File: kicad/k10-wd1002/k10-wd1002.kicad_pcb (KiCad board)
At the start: 2 copper layers, 139.7 x 114.3 mm, 10 parts, among them J1 J1 - Kaypro, J2 J2 - WD1002-HDO, U1 74LS00, U2 74LS138

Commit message: Refine K10-WD1002 PCB layout
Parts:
- moved J2 2.54 mm to (181.6, 142.2)
- moved C1 2.54 mm to (113.0, 91.4)
- moved J1 2.54 mm to (87.6, 127.0)
- moved R1 2.54 mm to (124.5, 94.0)
- moved U1 2.54 mm to (133.3, 94.0)
- moved U2 2.54 mm to (100.3, 91.4)
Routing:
- net (no net): track 3407.3 -> 3405.9 mm
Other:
- board text added: "1"
- board text added: "40"
- board text added: "50"
- board text added: "81-212A (2022)"
- board text added: "C1"
- board text added: "J1"
- board text added: "J2"
- board text added: "KAYPRO"
- board text added: "R1"
- board text added: "U1"
- board text added: "U2"
- board text added: "WD1002-05/HDO"

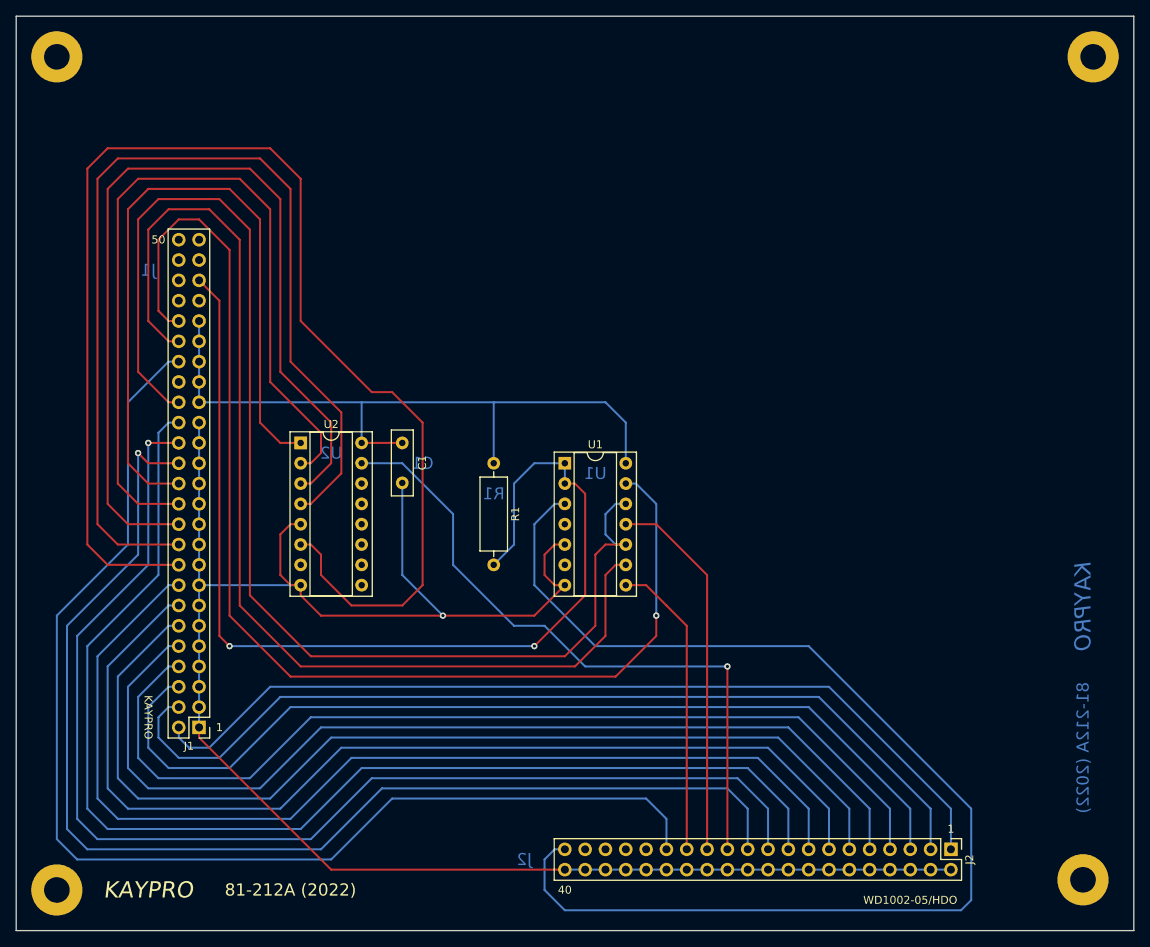
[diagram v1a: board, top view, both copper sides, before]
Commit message: Finish PCB layout
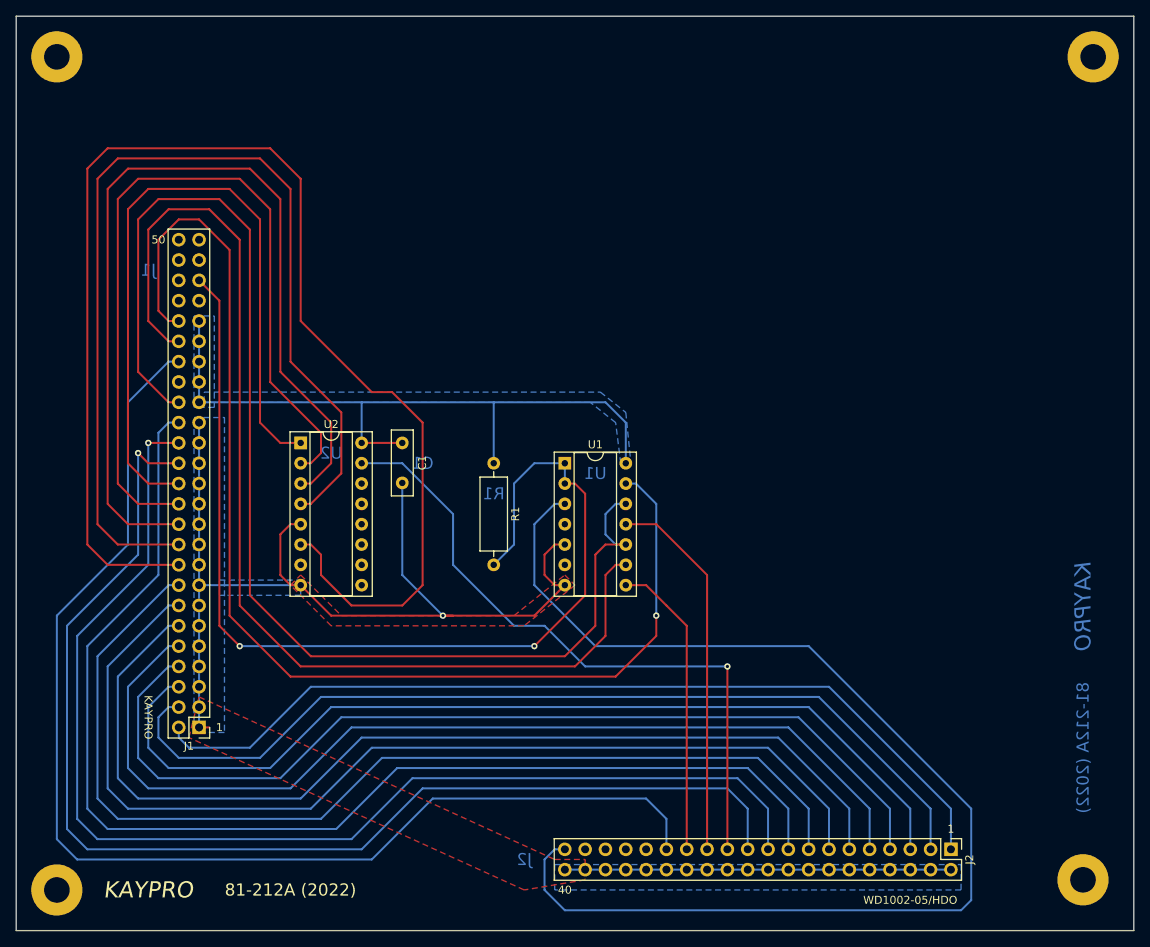
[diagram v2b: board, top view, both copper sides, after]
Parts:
- C1: value 0.1uF -> 0.1
- J1: value J1 - Kaypro -> Kaypro
- J2: value J2 - WD1002-HDO -> WD1002
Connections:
- C1 pad 1: (no net) -> VCC
- C1 pad 2: (no net) -> GND
- J1 pad 1: (no net) -> GND
- J1 pad 10: (no net) -> /BD4
- J1 pad 11: (no net) -> GND
- J1 pad 12: (no net) -> /BD5
- J1 pad 13: (no net) -> GND
- J1 pad 14: (no net) -> /BD6
- J1 pad 15: (no net) -> GND
- J1 pad 16: (no net) -> /BD7
- J1 pad 17: (no net) -> GND
- J1 pad 18: (no net) -> /BA7
- J1 pad 19: (no net) -> GND
- J1 pad 2: (no net) -> /BD0
- J1 pad 20: (no net) -> /BA6
- J1 pad 21: (no net) -> GND
- J1 pad 22: (no net) -> /BA5
- J1 pad 23: (no net) -> GND
- J1 pad 24: (no net) -> /BA4
- J1 pad 25: (no net) -> GND
- J1 pad 26: (no net) -> /BA3
- J1 pad 27: (no net) -> GND
- J1 pad 28: (no net) -> /BA2
- J1 pad 29: (no net) -> GND
- J1 pad 3: (no net) -> GND
- J1 pad 30: (no net) -> /BA1
- J1 pad 31: (no net) -> GND
- J1 pad 32: (no net) -> /BA0
- J1 pad 33: (no net) -> VCC
- J1 pad 34: (no net) -> /IORQ
- J1 pad 35: (no net) -> VCC
- J1 pad 36: (no net) -> /-M1
- J1 pad 37: (no net) -> VCC
- J1 pad 38: (no net) -> /-WAIT
- J1 pad 39: (no net) -> VCC
- J1 pad 4: (no net) -> /BD1
- J1 pad 40: (no net) -> /RD
- J1 pad 41: (no net) -> VCC
- J1 pad 42: (no net) -> /WR
- J1 pad 43: (no net) -> /-RESET
- J1 pad 44: (no net) -> /INT
- J1 pad 45: (no net) -> /-HDRST
- J1 pad 46: (no net) -> /IEO
- J1 pad 47: (no net) -> Net-(J1-Pad47)
- J1 pad 48: (no net) -> Net-(J1-Pad48)
- J1 pad 49: (no net) -> /4MHz
- J1 pad 5: (no net) -> GND
- J1 pad 50: (no net) -> Net-(J1-Pad50)
- J1 pad 6: (no net) -> /BD2
- J1 pad 7: (no net) -> GND
- J1 pad 8: (no net) -> /BD3
- J1 pad 9: (no net) -> GND
- J2 pad 1: (no net) -> /BD0
- J2 pad 10: (no net) -> GND
- J2 pad 11: (no net) -> /BD5
- J2 pad 12: (no net) -> GND
- J2 pad 13: (no net) -> /BD6
- J2 pad 14: (no net) -> GND
- J2 pad 15: (no net) -> /BD7
- J2 pad 16: (no net) -> GND
- J2 pad 17: (no net) -> /BA0
- J2 pad 18: (no net) -> GND
- J2 pad 19: (no net) -> /BA1
- J2 pad 2: (no net) -> GND
- J2 pad 20: (no net) -> GND
- J2 pad 21: (no net) -> /BA2
- J2 pad 22: (no net) -> GND
- J2 pad 23: (no net) -> /-CS
- J2 pad 24: (no net) -> GND
- J2 pad 25: (no net) -> /-WE
- J2 pad 26: (no net) -> GND
- J2 pad 27: (no net) -> /-RE
- J2 pad 28: (no net) -> GND
- J2 pad 29: (no net) -> /-WAIT
- J2 pad 3: (no net) -> /BD1
- J2 pad 30: (no net) -> GND
- J2 pad 31: (no net) -> Net-(J2-Pad31)
- J2 pad 32: (no net) -> GND
- J2 pad 33: (no net) -> Net-(J2-Pad33)
- J2 pad 34: (no net) -> GND
- J2 pad 35: (no net) -> /INTRQ
- J2 pad 36: (no net) -> GND
- J2 pad 37: (no net) -> /DRQ
- J2 pad 38: (no net) -> GND
- J2 pad 39: (no net) -> /-MR
- J2 pad 4: (no net) -> GND
- J2 pad 40: (no net) -> GND
- J2 pad 5: (no net) -> /BD2
- J2 pad 6: (no net) -> GND
- J2 pad 7: (no net) -> /BD3
- J2 pad 8: (no net) -> GND
- J2 pad 9: (no net) -> /BD4
- R1 pad 1: (no net) -> VCC
- R1 pad 2: (no net) -> /-HDRST
- U1 pad 1: (no net) -> /-HDRST
- U1 pad 10: (no net) -> /IORQ
- U1 pad 11: (no net) -> /-WE
- U1 pad 12: (no net) -> /IORQ
- U1 pad 13: (no net) -> /WR
- U1 pad 14: (no net) -> VCC
- U1 pad 2: (no net) -> /-HDRST
- U1 pad 3: (no net) -> /-MR
- U1 pad 4: (no net) -> Net-(U1-Pad4)
- U1 pad 5: (no net) -> GND
- U1 pad 6: (no net) -> Net-(U1-Pad6)
- U1 pad 7: (no net) -> GND
- U1 pad 8: (no net) -> /-RE
- U1 pad 9: (no net) -> /RD
- U2 pad 1: (no net) -> /BA3
- U2 pad 10: (no net) -> Net-(U2-Pad10)
- U2 pad 11: (no net) -> Net-(U2-Pad11)
- U2 pad 12: (no net) -> Net-(U2-Pad12)
- U2 pad 13: (no net) -> Net-(U2-Pad13)
- U2 pad 14: (no net) -> Net-(U2-Pad14)
- U2 pad 15: (no net) -> /-CS
- U2 pad 16: (no net) -> VCC
- U2 pad 2: (no net) -> /BA4
- U2 pad 3: (no net) -> /BA5
- U2 pad 4: (no net) -> /BA6
- U2 pad 5: (no net) -> GND
- U2 pad 6: (no net) -> /BA7
- U2 pad 7: (no net) -> Net-(U2-Pad7)
- U2 pad 8: (no net) -> GND
- U2 pad 9: (no net) -> Net-(U2-Pad9)
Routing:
- net (no net): track 3405.9 -> 0.00 mm, vias 7 -> 0
- net GND: track 0.00 -> 176.4 mm, vias 0 -> 1
- net /BA7: track 0.00 -> 168.3 mm
- net /IORQ: track 0.00 -> 157.8 mm
- net /BA0: track 0.00 -> 152.8 mm
- net /-WAIT: track 0.00 -> 152.0 mm
- net /-MR: track 0.00 -> 151.9 mm
- net /BA2: track 0.00 -> 151.7 mm, vias 0 -> 1
- net /BA1: track 0.00 -> 151.7 mm, vias 0 -> 1
- net /WR: track 0.00 -> 149.2 mm, vias 0 -> 1
- net /RD: track 0.00 -> 137.2 mm
- net /BD7: track 0.00 -> 132.4 mm
- net /-HDRST: track 0.00 -> 130.6 mm, vias 0 -> 2
- net /BD6: track 0.00 -> 129.9 mm
- net /BD5: track 0.00 -> 127.4 mm
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- added copper zone on B.Cu, net GND
- added copper zone on F.Cu, net GND
- added copper zone on B.Cu, net VCC

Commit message: k10-wd1002: make trace width 0.025 and cleanup
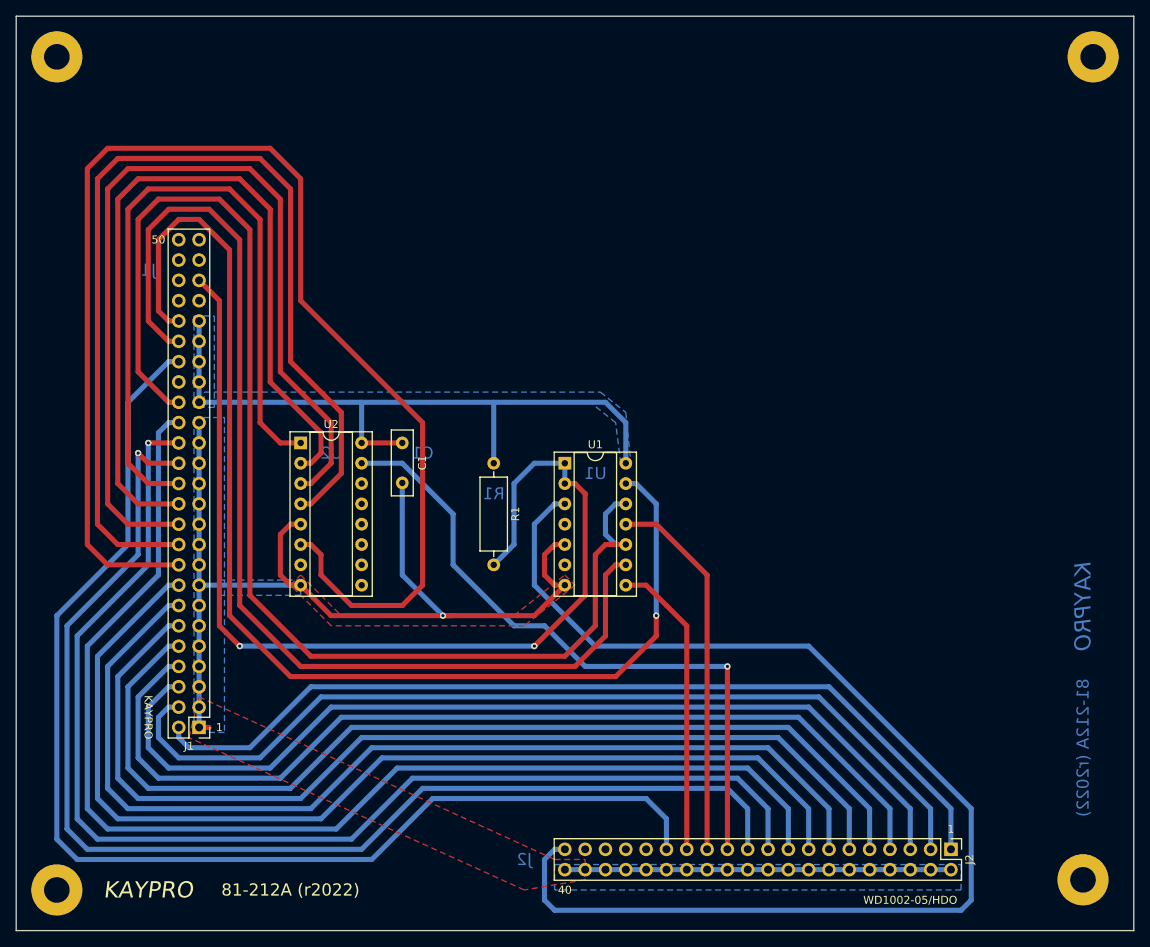
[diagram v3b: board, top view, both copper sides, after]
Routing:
- net /BA7: track 168.3 -> 166.8 mm
- net /-MR: track 151.9 -> 152.6 mm
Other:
- board text added: "81-212A (r2022)"
- board text removed: "81-212A (2022)"

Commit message: Fix mounting holes and cleanup GND zones
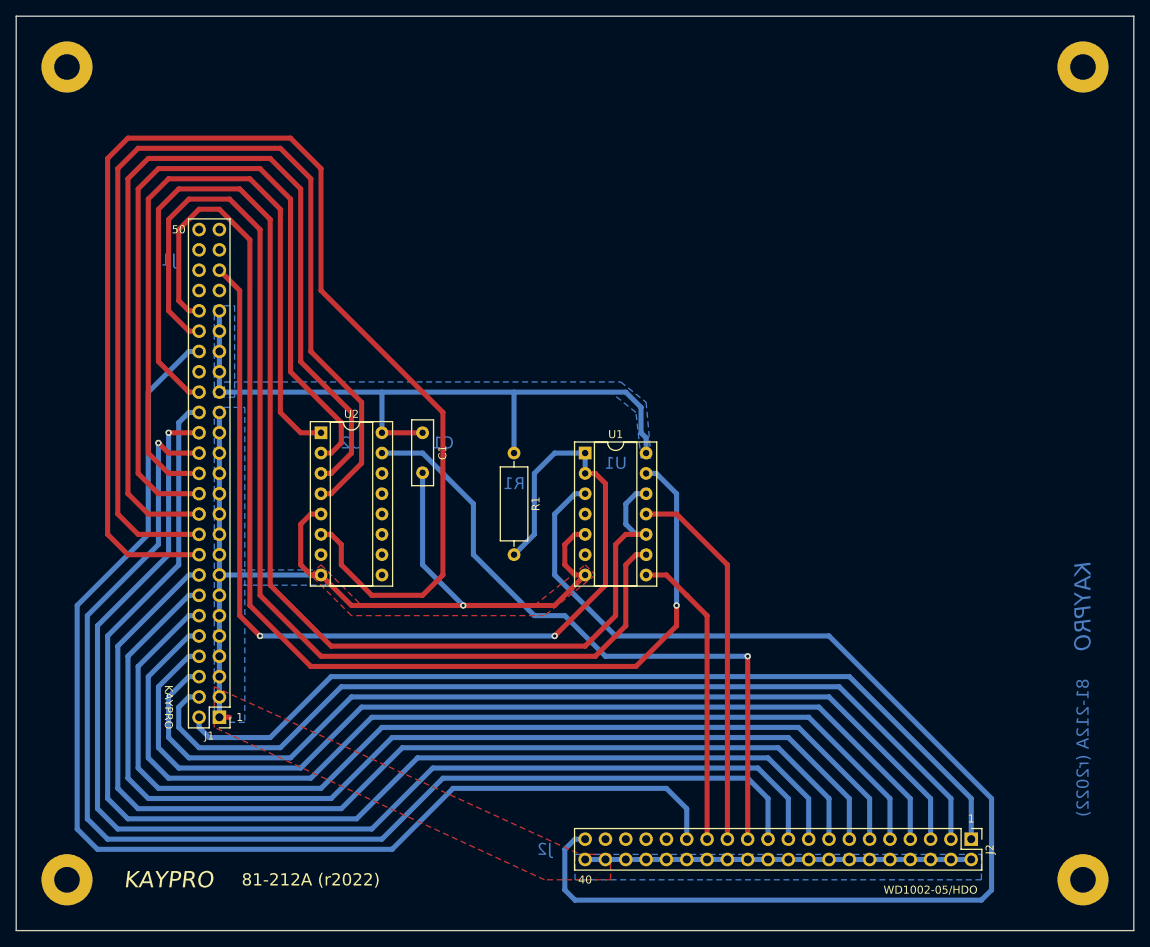
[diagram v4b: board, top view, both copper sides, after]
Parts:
- moved R1 2.84 mm to (127.0, 92.7)
- moved J1 2.84 mm to (90.2, 125.7)
- moved U2 2.84 mm to (102.9, 90.2)
- moved J2 2.84 mm to (184.2, 141.0)
- moved U1 2.84 mm to (135.9, 92.7)
- moved C1 2.84 mm to (115.6, 90.2)
- moved   1.80 mm to (71.1, 44.5)
- moved   1.80 mm to (71.1, 146.1)
- moved   1.80 mm to (198.1, 44.5)
